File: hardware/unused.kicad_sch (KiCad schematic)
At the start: 6 parts, among them U10 74HCS08, U13 74HC74, U2 74AC04SC, U9 74HCS32

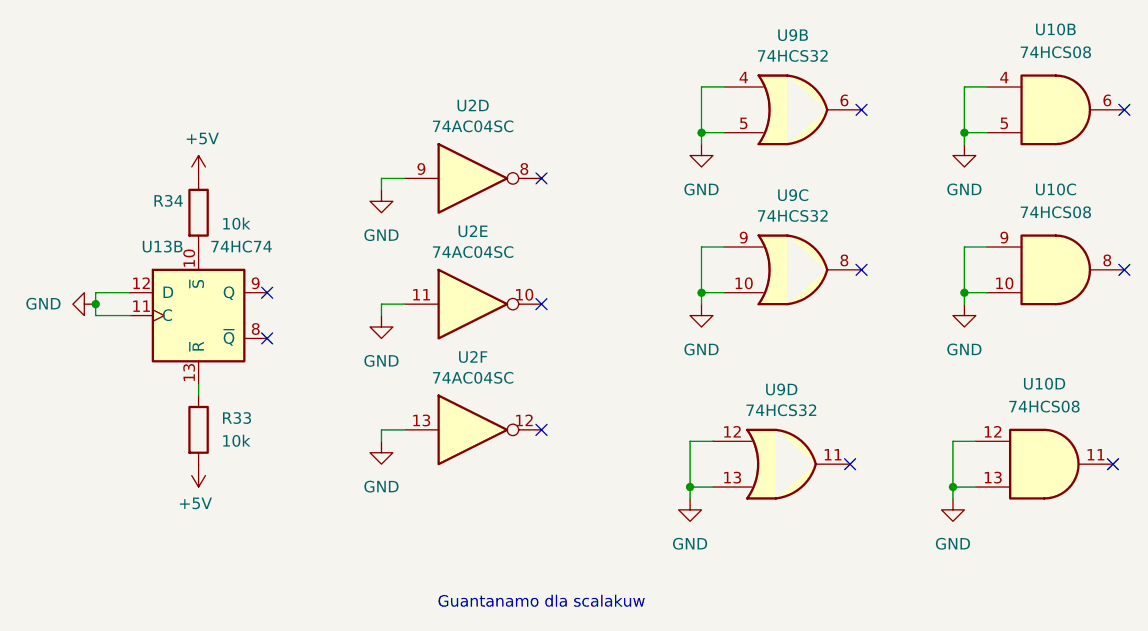
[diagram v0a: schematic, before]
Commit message: Add input stage LM393 comment
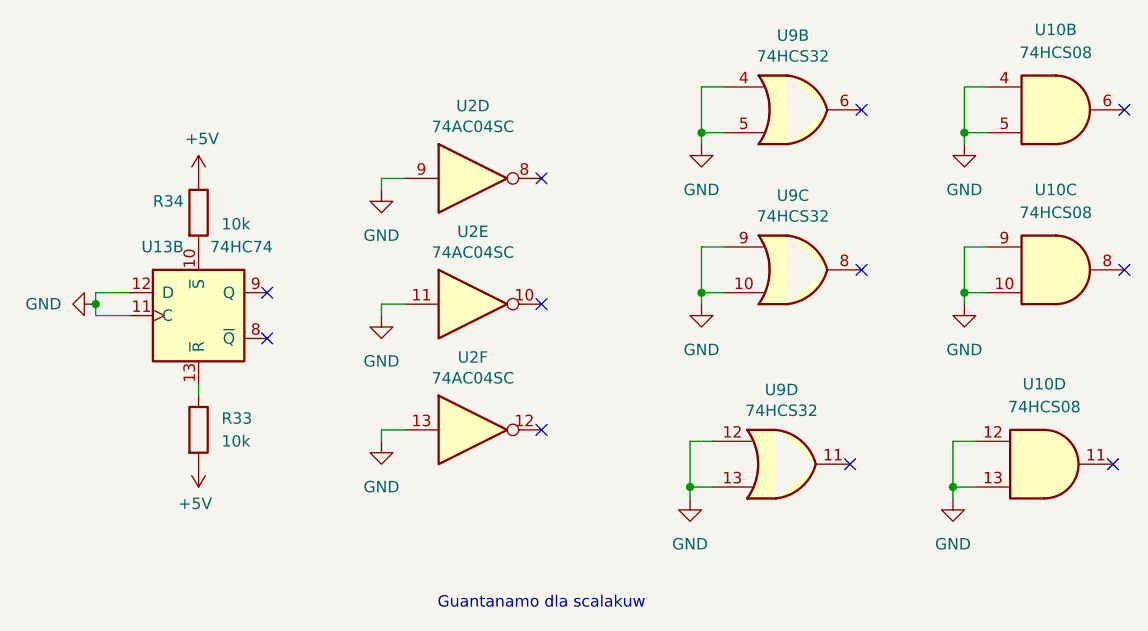
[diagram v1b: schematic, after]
